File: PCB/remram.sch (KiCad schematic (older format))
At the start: 0 parts

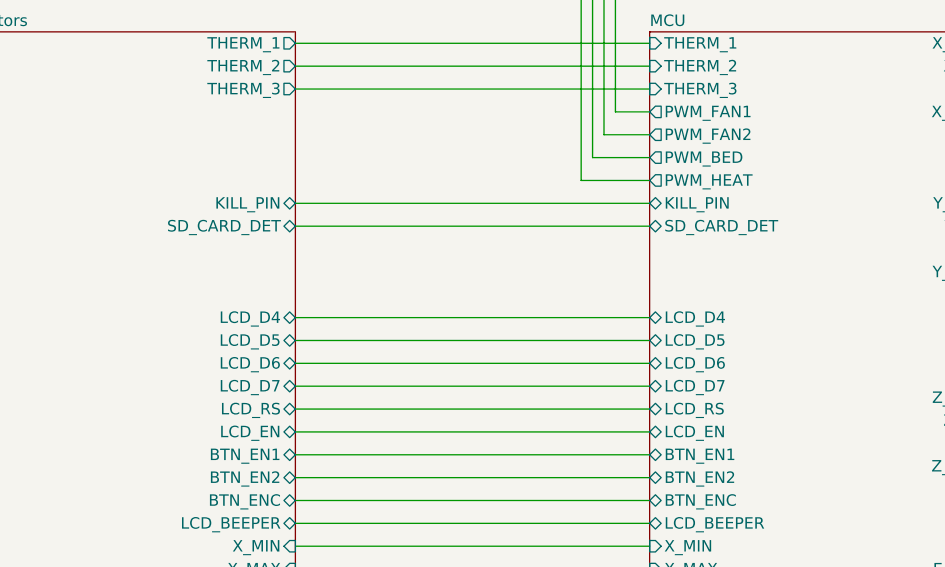
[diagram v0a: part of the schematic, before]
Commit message: v0.2 of PCB.
After some feedback, we changed following:
 - Switched FAN VDD from 24 to 5V.
 - FAN now have a ADC pin for speed sensing.
 - Expanded EXP-3 connector to 26 pin
   - Included 24V VDD.
   - Could be used to connect up to two
     extra stepper.
 - Removed GND connections on TMC2130 to
   middel GND plane.
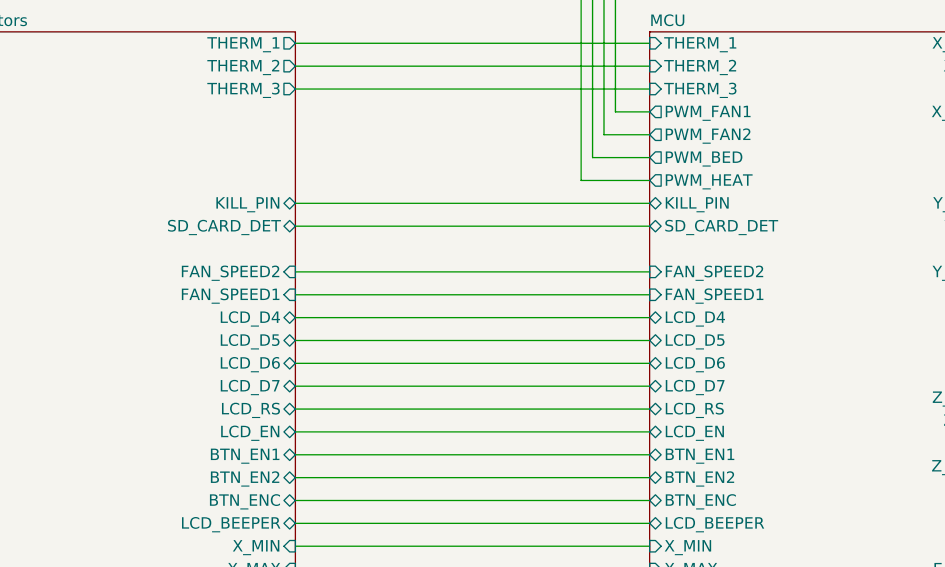
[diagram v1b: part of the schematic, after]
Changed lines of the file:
@@
 F68 "PWM_EXT4" I L 6200 5350 50
 F69 "PWM_EXT1" I L 6200 5050 50
+F70 "FAN_SPEED1" I L 6200 2000 50
+F71 "FAN_SPEED2" I L 6200 1900 50
 $EndSheet
 $Sheet
@@
 F50 "PWM_EXT3" I R 4650 5250 50
 F51 "PWM_EXT4" I R 4650 5350 50
+F52 "FAN_SPEED1" I R 4650 2000 50
+F53 "FAN_SPEED2" I R 4650 1900 50
 $EndSheet
 $Sheet
@@
 Wire Wire Line
 	8250 5400 8250 5100
+Wire Wire Line
+	4650 1900 6200 1900
+Wire Wire Line
+	6200 2000 4650 2000
 $EndSCHEMATC

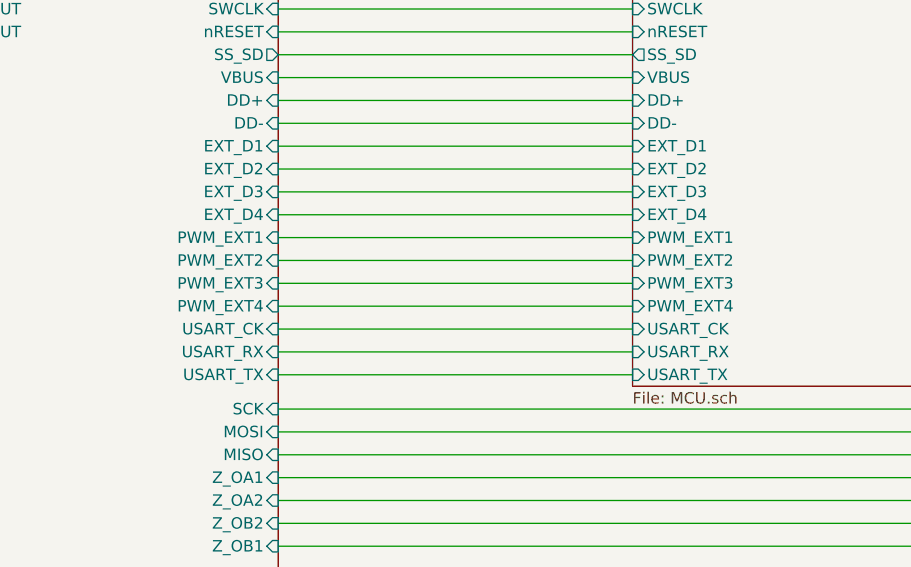
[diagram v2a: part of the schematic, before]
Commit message: Removed USART1 CK pin and added another digial pin.
STM32duino doesn't seem to support USART. So I will only
implement the UART pins.
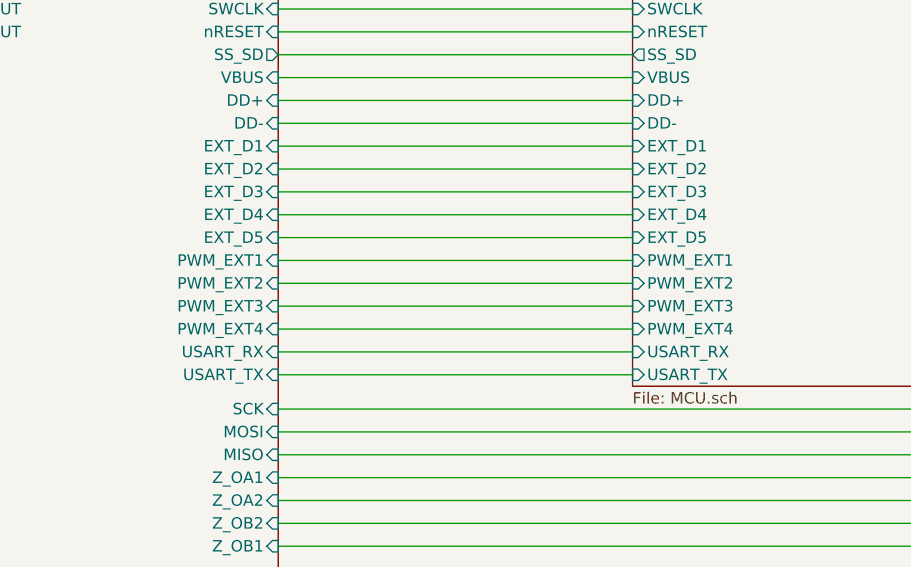
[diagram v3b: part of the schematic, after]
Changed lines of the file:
@@
 F61 "EXT_D4" I L 6200 4950 50
 F62 "EXT_D3" I L 6200 4850 50
-F63 "PWM_EXT2" I L 6200 5150 50
-F64 "PWM_EXT3" I L 6200 5250 50
+F63 "PWM_EXT2" I L 6200 5250 50
+F64 "PWM_EXT3" I L 6200 5350 50
 F65 "USART_RX" I L 6200 5550 50
 F66 "USART_TX" I L 6200 5650 50
-F67 "USART_CK" I L 6200 5450 50
-F68 "PWM_EXT4" I L 6200 5350 50
-F69 "PWM_EXT1" I L 6200 5050 50
-F70 "FAN_SPEED1" I L 6200 2000 50
-F71 "FAN_SPEED2" I L 6200 1900 50
+F67 "PWM_EXT4" I L 6200 5450 50
+F68 "PWM_EXT1" I L 6200 5150 50
+F69 "FAN_SPEED1" I L 6200 2000 50
+F70 "FAN_SPEED2" I L 6200 1900 50
+F71 "EXT_D5" I L 6200 5050 50
 $EndSheet
 $Sheet
@@
 F43 "USART_TX" I R 4650 5650 50
 F44 "USART_RX" I R 4650 5550 50
-F45 "USART_CK" I R 4650 5450 50
-F46 "PWM_EXT1" I R 4650 5050 50
-F47 "PWM_EXT2" I R 4650 5150 50
-F48 "EXT_D3" I R 4650 4850 50
-F49 "EXT_D4" I R 4650 4950 50
-F50 "PWM_EXT3" I R 4650 5250 50
-F51 "PWM_EXT4" I R 4650 5350 50
-F52 "FAN_SPEED1" I R 4650 2000 50
-F53 "FAN_SPEED2" I R 4650 1900 50
+F45 "PWM_EXT1" I R 4650 5150 50
+F46 "PWM_EXT2" I R 4650 5250 50
+F47 "EXT_D3" I R 4650 4850 50
+F48 "EXT_D4" I R 4650 4950 50
+F49 "PWM_EXT3" I R 4650 5350 50
+F50 "PWM_EXT4" I R 4650 5450 50
+F51 "FAN_SPEED1" I R 4650 2000 50
+F52 "FAN_SPEED2" I R 4650 1900 50
+F53 "EXT_D5" I R 4650 5050 50
 $EndSheet
 $Sheet
@@
 	6200 5350 4650 5350
 Wire Wire Line
-	4650 5450 6200 5450
-Wire Wire Line
 	6200 5550 4650 5550
 Wire Wire Line
@@
 Wire Wire Line
 	6200 2000 4650 2000
+Wire Wire Line
+	4650 5450 6200 5450
 $EndSCHEMATC

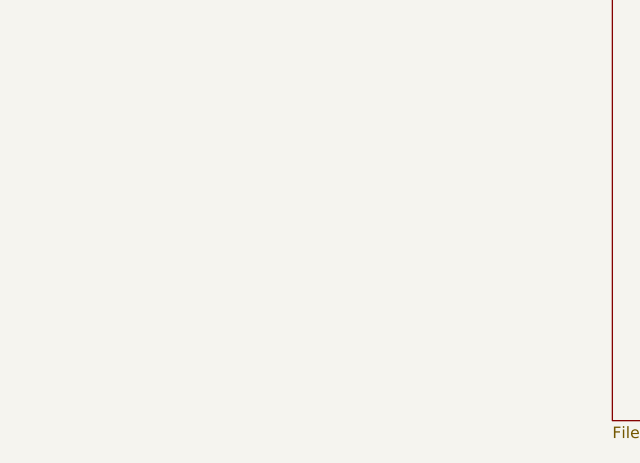
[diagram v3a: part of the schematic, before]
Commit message: Add Schmitt Trigger for fan tachometer
The fan tachometer is too noise for the STM32F7 3.3V IO.
We need to add a Schmitt Trigger to have a better noise handling
and gain more low/high margin.

Also some minor silkscreen adjustments. Backward compatible
with v1.0.wq
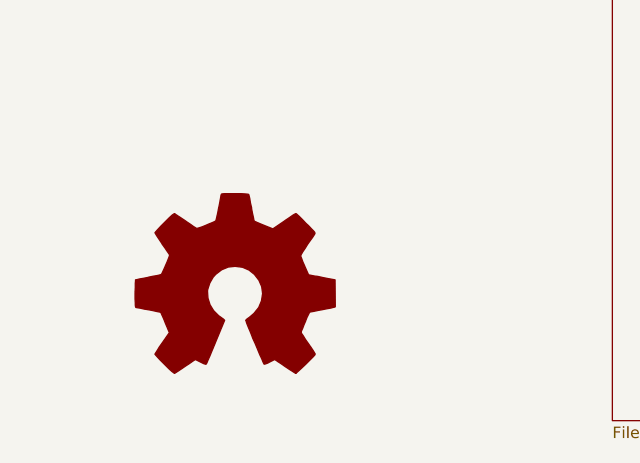
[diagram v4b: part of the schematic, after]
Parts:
- added LOGO1: Logo_Open_Hardware_Large, Symbol:OSHW-Logo2_14.6x12mm_SilkScreen, symbol Graphic:Logo_Open_Hardware_Large
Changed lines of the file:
@@
 Wire Wire Line
 	4650 5450 6200 5450
+$Comp
+L Graphic:Logo_Open_Hardware_Large LOGO1
+U 1 1 5B5A8FFB
+P 1450 7000
+F 0 "LOGO1" H 1450 7500 50  0001 C CNN
+F 1 "Logo_Open_Hardware_Large" H 1450 6600 50  0001 C CNN
+F 2 "Symbol:OSHW-Logo2_14.6x12mm_SilkScreen" H 1450 7516 50  0001 C CNN
+F 3 "~" H 1450 7000 50  0001 C CNN
+	1    1450 7000
+	1    0    0    -1
+$EndComp
 $EndSCHEMATC

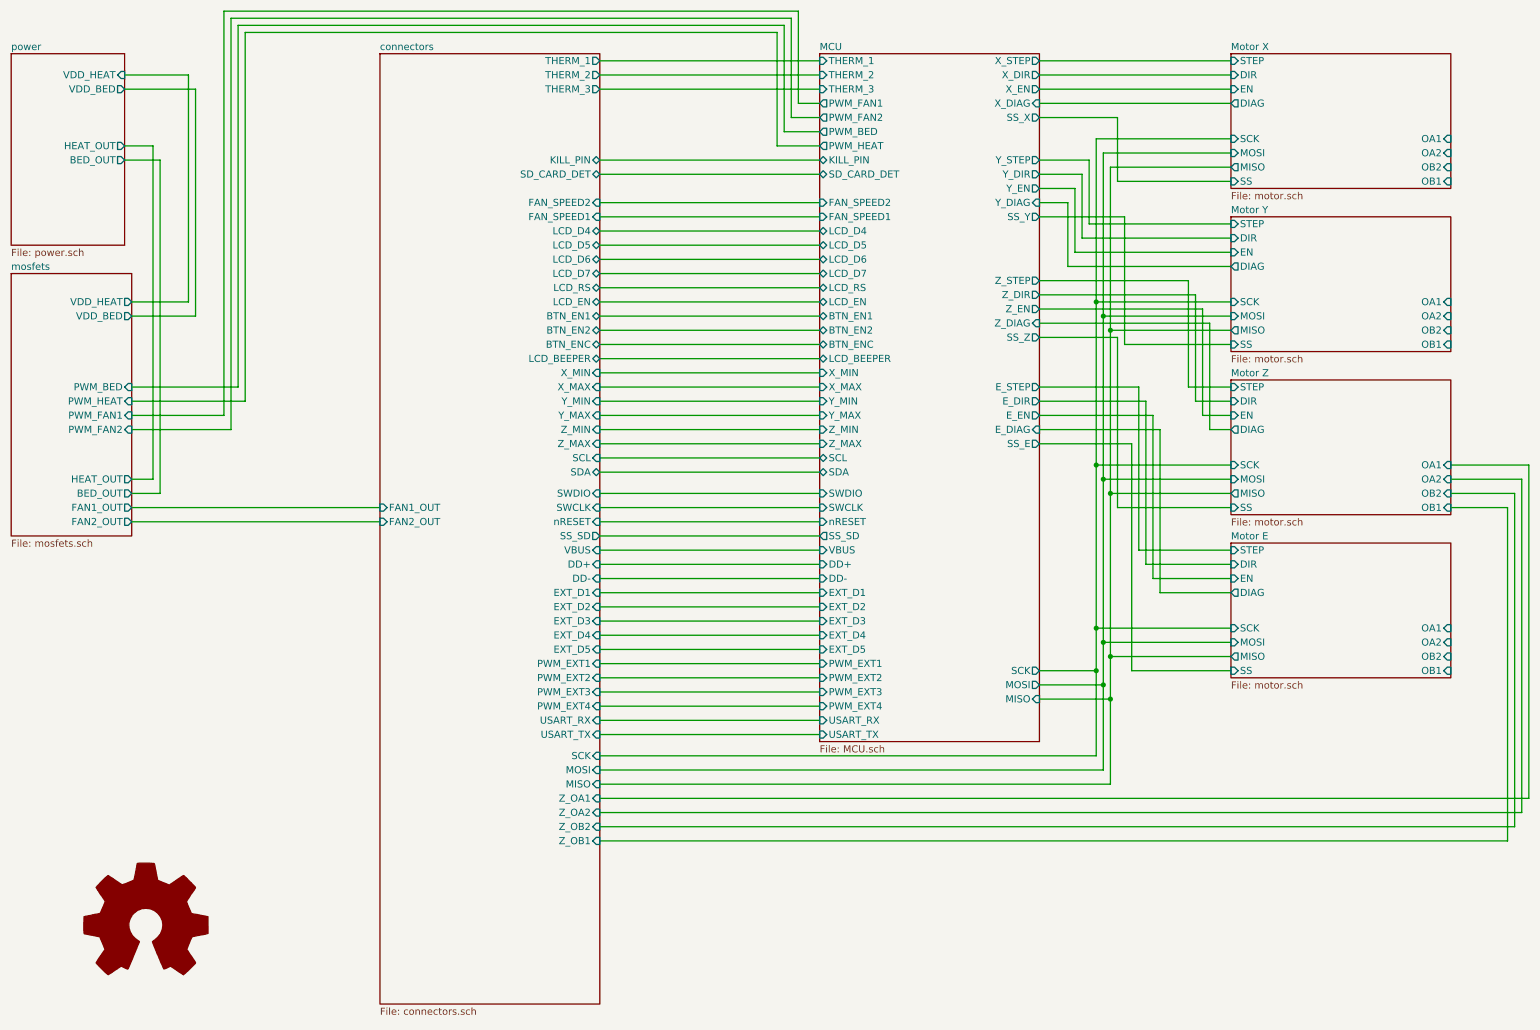
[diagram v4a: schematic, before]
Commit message: Add micro SD card reader and finished GND stitching
Just to be safe, the SD card reader got it's own LDO.
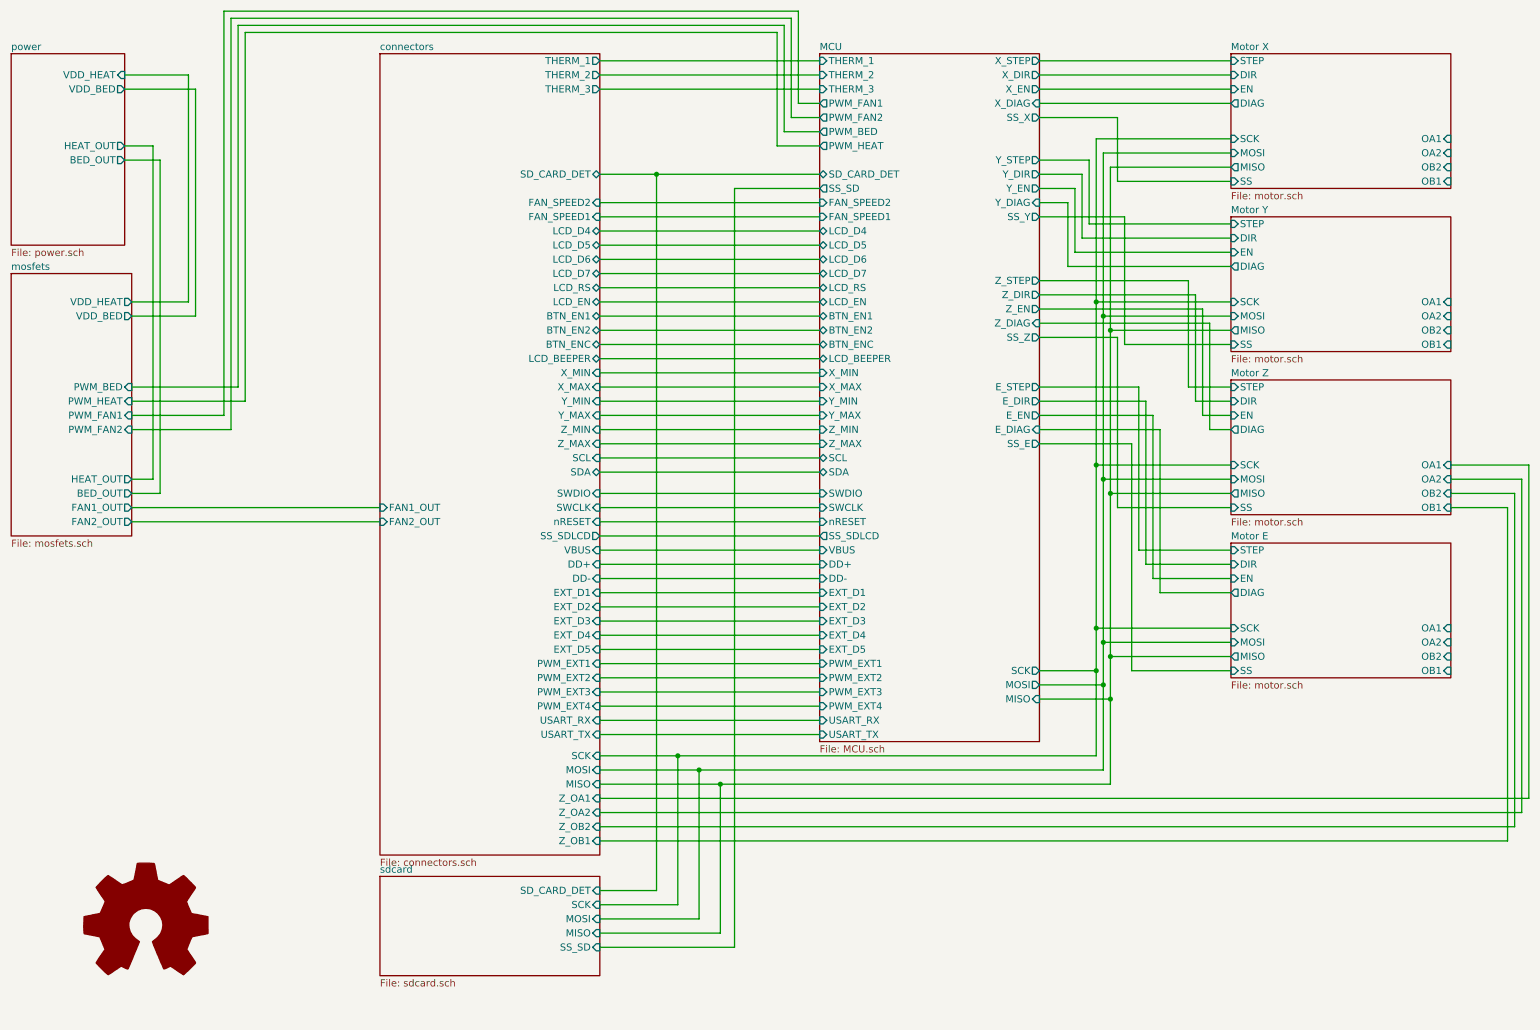
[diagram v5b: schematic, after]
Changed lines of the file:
@@
 $Descr A4 11693 8268
 encoding utf-8
-Sheet 1 9
+Sheet 1 10
 Title "Overview"
 Date ""
@@
 	1350 3400 2000 3400
 Wire Wire Line
-	4650 1600 6200 1600
-Wire Wire Line
-	6200 1700 4650 1700
+	6200 1700 5050 1700
 Wire Wire Line
 	6200 2100 4650 2100
@@
 F38 "SS_Z" O R 7750 2850 50
 F39 "SS_E" O R 7750 3600 50
-F40 "SS_SD" O L 6200 4250 50
-F41 "KILL_PIN" B L 6200 1600 50
-F42 "SD_CARD_DET" B L 6200 1700 50
-F43 "LCD_D6" B L 6200 2300 50
-F44 "LCD_D7" B L 6200 2400 50
-F45 "EXT_D1" I L 6200 4650 50
-F46 "EXT_D2" I L 6200 4750 50
-F47 "LCD_D5" B L 6200 2200 50
-F48 "LCD_D4" B L 6200 2100 50
-F49 "LCD_RS" B L 6200 2500 50
-F50 "LCD_EN" B L 6200 2600 50
-F51 "BTN_EN2" B L 6200 2800 50
-F52 "BTN_ENC" B L 6200 2900 50
-F53 "BTN_EN1" B L 6200 2700 50
-F54 "X_MIN" I L 6200 3100 50
-F55 "X_MAX" I L 6200 3200 50
-F56 "Y_MIN" I L 6200 3300 50
-F57 "Y_MAX" I L 6200 3400 50
-F58 "Z_MIN" I L 6200 3500 50
-F59 "Z_MAX" I L 6200 3600 50
-F60 "LCD_BEEPER" B L 6200 3000 50
-F61 "EXT_D4" I L 6200 4950 50
-F62 "EXT_D3" I L 6200 4850 50
-F63 "PWM_EXT2" I L 6200 5250 50
-F64 "PWM_EXT3" I L 6200 5350 50
-F65 "USART_RX" I L 6200 5550 50
-F66 "USART_TX" I L 6200 5650 50
-F67 "PWM_EXT4" I L 6200 5450 50
-F68 "PWM_EXT1" I L 6200 5150 50
-F69 "FAN_SPEED1" I L 6200 2000 50
-F70 "FAN_SPEED2" I L 6200 1900 50
-F71 "EXT_D5" I L 6200 5050 50
-$EndSheet
-$Sheet
-S 3100 850  1550 6700
+F40 "SS_SD" O L 6200 1800 50
+F41 "SD_CARD_DET" B L 6200 1700 50
+F42 "LCD_D6" B L 6200 2300 50
+F43 "LCD_D7" B L 6200 2400 50
+F44 "EXT_D1" I L 6200 4650 50
+F45 "EXT_D2" I L 6200 4750 50
+F46 "LCD_D5" B L 6200 2200 50
+F47 "LCD_D4" B L 6200 2100 50
+F48 "LCD_RS" B L 6200 2500 50
+F49 "LCD_EN" B L 6200 2600 50
+F50 "BTN_EN2" B L 6200 2800 50
+F51 "BTN_ENC" B L 6200 2900 50
+F52 "BTN_EN1" B L 6200 2700 50
+F53 "X_MIN" I L 6200 3100 50
+F54 "X_MAX" I L 6200 3200 50
+F55 "Y_MIN" I L 6200 3300 50
+F56 "Y_MAX" I L 6200 3400 50
+F57 "Z_MIN" I L 6200 3500 50
+F58 "Z_MAX" I L 6200 3600 50
+F59 "LCD_BEEPER" B L 6200 3000 50
+F60 "EXT_D4" I L 6200 4950 50
+F61 "EXT_D3" I L 6200 4850 50
+F62 "PWM_EXT2" I L 6200 5250 50
+F63 "PWM_EXT3" I L 6200 5350 50
+F64 "USART_RX" I L 6200 5550 50
+F65 "USART_TX" I L 6200 5650 50
+F66 "PWM_EXT4" I L 6200 5450 50
+F67 "PWM_EXT1" I L 6200 5150 50
+F68 "FAN_SPEED1" I L 6200 2000 50
+F69 "FAN_SPEED2" I L 6200 1900 50
+F70 "EXT_D5" I L 6200 5050 50
+F71 "SS_SDLCD" O L 6200 4250 50
+$EndSheet
+$Sheet
+S 3100 850  1550 5650
 U 5AF74780
 F0 "connectors" 50
@@
 F13 "FAN1_OUT" I L 3100 4050 50
 F14 "FAN2_OUT" I L 3100 4150 50
-F15 "SS_SD" O R 4650 4250 50
-F16 "LCD_D5" B R 4650 2200 50
-F17 "LCD_D4" B R 4650 2100 50
-F18 "LCD_RS" B R 4650 2500 50
-F19 "LCD_EN" B R 4650 2600 50
-F20 "BTN_EN2" B R 4650 2800 50
-F21 "BTN_ENC" B R 4650 2900 50
-F22 "LCD_BEEPER" B R 4650 3000 50
-F23 "BTN_EN1" B R 4650 2700 50
-F24 "KILL_PIN" B R 4650 1600 50
-F25 "SD_CARD_DET" B R 4650 1700 50
-F26 "Z_MAX" I R 4650 3600 50
-F27 "Z_MIN" I R 4650 3500 50
-F28 "Y_MAX" I R 4650 3400 50
-F29 "Y_MIN" I R 4650 3300 50
-F30 "X_MAX" I R 4650 3200 50
-F31 "X_MIN" I R 4650 3100 50
-F32 "SCK" I R 4650 5800 50
-F33 "MISO" I R 4650 6000 50
-F34 "MOSI" I R 4650 5900 50
-F35 "LCD_D6" B R 4650 2300 50
-F36 "LCD_D7" B R 4650 2400 50
-F37 "EXT_D1" I R 4650 4650 50
-F38 "EXT_D2" I R 4650 4750 50
-F39 "Z_OA1" I R 4650 6100 50
-F40 "Z_OA2" I R 4650 6200 50
-F41 "Z_OB2" I R 4650 6300 50
-F42 "Z_OB1" I R 4650 6400 50
-F43 "USART_TX" I R 4650 5650 50
-F44 "USART_RX" I R 4650 5550 50
-F45 "PWM_EXT1" I R 4650 5150 50
-F46 "PWM_EXT2" I R 4650 5250 50
-F47 "EXT_D3" I R 4650 4850 50
-F48 "EXT_D4" I R 4650 4950 50
-F49 "PWM_EXT3" I R 4650 5350 50
-F50 "PWM_EXT4" I R 4650 5450 50
-F51 "FAN_SPEED1" I R 4650 2000 50
-F52 "FAN_SPEED2" I R 4650 1900 50
-F53 "EXT_D5" I R 4650 5050 50
+F15 "LCD_D5" B R 4650 2200 50
+F16 "LCD_D4" B R 4650 2100 50
+F17 "LCD_RS" B R 4650 2500 50
+F18 "LCD_EN" B R 4650 2600 50
+F19 "BTN_EN2" B R 4650 2800 50
+F20 "BTN_ENC" B R 4650 2900 50
+F21 "LCD_BEEPER" B R 4650 3000 50
+F22 "BTN_EN1" B R 4650 2700 50
+F23 "SD_CARD_DET" B R 4650 1700 50
+F24 "Z_MAX" I R 4650 3600 50
+F25 "Z_MIN" I R 4650 3500 50
+F26 "Y_MAX" I R 4650 3400 50
+F27 "Y_MIN" I R 4650 3300 50
+F28 "X_MAX" I R 4650 3200 50
+F29 "X_MIN" I R 4650 3100 50
+F30 "SCK" I R 4650 5800 50
+F31 "MISO" I R 4650 6000 50
+F32 "MOSI" I R 4650 5900 50
+F33 "LCD_D6" B R 4650 2300 50
+F34 "LCD_D7" B R 4650 2400 50
+F35 "EXT_D1" I R 4650 4650 50
+F36 "EXT_D2" I R 4650 4750 50
+F37 "Z_OA1" I R 4650 6100 50
+F38 "Z_OA2" I R 4650 6200 50
+F39 "Z_OB2" I R 4650 6300 50
+F40 "Z_OB1" I R 4650 6400 50
+F41 "USART_TX" I R 4650 5650 50
+F42 "USART_RX" I R 4650 5550 50
+F43 "PWM_EXT1" I R 4650 5150 50
+F44 "PWM_EXT2" I R 4650 5250 50
+F45 "EXT_D3" I R 4650 4850 50
+F46 "EXT_D4" I R 4650 4950 50
+F47 "PWM_EXT3" I R 4650 5350 50
+F48 "PWM_EXT4" I R 4650 5450 50
+F49 "FAN_SPEED1" I R 4650 2000 50
+F50 "FAN_SPEED2" I R 4650 1900 50
+F51 "EXT_D5" I R 4650 5050 50
+F52 "SS_SDLCD" O R 4650 4250 50
 $EndSheet
 $Sheet
@@
 	6200 4250 4650 4250
 Wire Wire Line
-	4650 5800 8150 5800
-Wire Wire Line
-	4650 5900 8200 5900
-Wire Wire Line
-	4650 6000 8250 6000
+	4650 5800 5200 5800
+Wire Wire Line
+	4650 5900 5350 5900
+Wire Wire Line
+	4650 6000 5500 6000
 Wire Wire Line
 	7750 5200 8150 5200
@@
 	1    0    0    -1
 $EndComp
+$Sheet
+S 3100 6650 1550 700
+U 5BB9460B
+F0 "sdcard" 50
+F1 "sdcard.sch" 50
+F2 "SD_CARD_DET" I R 4650 6750 50
+F3 "MOSI" I R 4650 6950 50
+F4 "MISO" I R 4650 7050 50
+F5 "SCK" I R 4650 6850 50
+F6 "SS_SD" I R 4650 7150 50
+$EndSheet
+Wire Wire Line
+	4650 6750 5050 6750
+Wire Wire Line
+	5050 6750 5050 1700
+Connection ~ 5050 1700
+Wire Wire Line
+	5050 1700 4650 1700
+Wire Wire Line
+	4650 6850 5200 6850
+Wire Wire Line
+	5200 6850 5200 5800
+Connection ~ 5200 5800
+Wire Wire Line
+	5200 5800 8150 5800
+Wire Wire Line
+	4650 6950 5350 6950
+Wire Wire Line
+	5350 6950 5350 5900
+Connection ~ 5350 5900
+Wire Wire Line
+	5350 5900 8200 5900
+Connection ~ 5500 6000
+Wire Wire Line
+	5500 6000 8250 6000
+Wire Wire Line
+	4650 7050 5500 7050
+Wire Wire Line
+	5500 6000 5500 7050
+Wire Wire Line
+	4650 7150 5600 7150
+Wire Wire Line
+	5600 7150 5600 1800
+Wire Wire Line
+	5600 1800 6200 1800
 $EndSCHEMATC
